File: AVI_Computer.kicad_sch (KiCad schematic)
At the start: 14 parts, among them IC1 ESP32-S2-MINI-2U-N4, IC2 LM3671MF-3.3_NOPB, IC3 LM3671MF-3.3_NOPB, IC4 BMP390, IC5 BMI270, J1 USB4105-GF-A-060

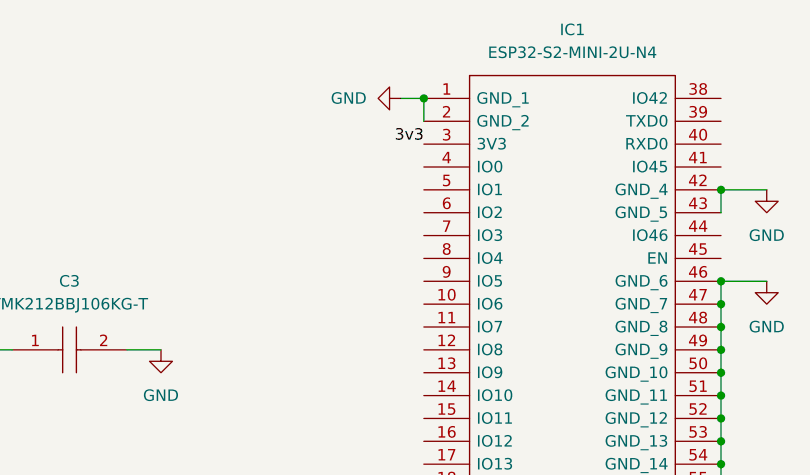
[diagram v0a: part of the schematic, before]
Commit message: i2c connection
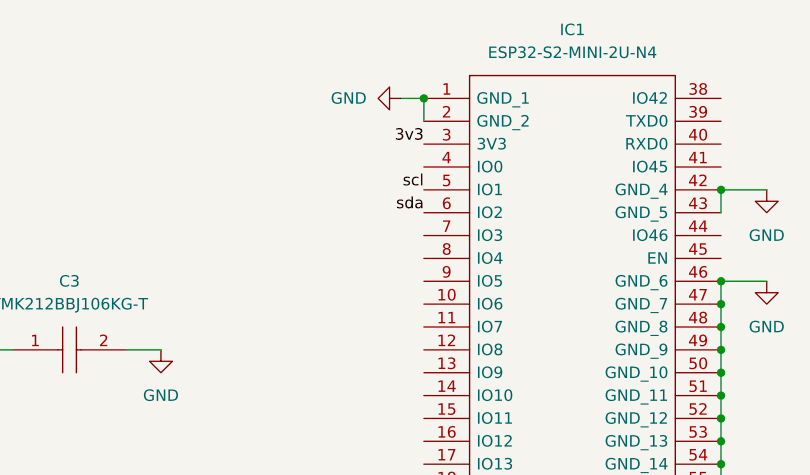
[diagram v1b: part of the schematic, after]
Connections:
- net scl: now also IC1.5 (IO1)
- net sda: now also IC1.6 (IO2)
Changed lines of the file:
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@@
     (effects (font (size 1.27 1.27)) (justify left bottom))
+  )
+  (label "scl" (at 142.24 40.64 180) (fields_autoplaced)
+    (effects (font (size 1.27 1.27)) (justify right bottom))
   )
   (label "D-" (at 137.16 86.36 180) (fields_autoplaced)
@@
     (effects (font (size 1.27 1.27)) (justify right bottom))
   )
+  (label "sda" (at 142.24 43.18 180) (fields_autoplaced)
+    (effects (font (size 1.27 1.27)) (justify right bottom))
+  )
